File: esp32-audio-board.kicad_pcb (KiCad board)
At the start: 4 copper layers, 37.5 x 70 mm, 125 parts, among them IC1 LP2985A-33DBVR, J1 EN_PAD0, J10 PWR_LED+, J11 HP_LOUT1, J12 HP_ROUT1, J13 HP_LOUT2, J14 HP_ROUT2, J15 MIC_LIN1, J16 MIC_LIN1_GND, J17 MIC_RIN1, J18 MIC_RIN1_GND, J19 HP_GND1, J2 JST S2B, J20 HP_GND2, J21 VP_PAD0, J22 PWR_LED-, J23 CHG_LED+, J24 CHG_LED-, J3 USB_C_Receptacle_USB2.0_16P, J4 EN_PAD1, J5 VP_PAD1, J6 VN_PAD0, J7 VN_PAD1, J8 IO34_PAD0, J9 IO34_PAD1, Q1 SS8050, Q2 SS8050, Q4 AO3401A, U1 ESP32-WROOM-32E, U2 CP2102, U3 MCP73831-2-OT, U5 ES8388

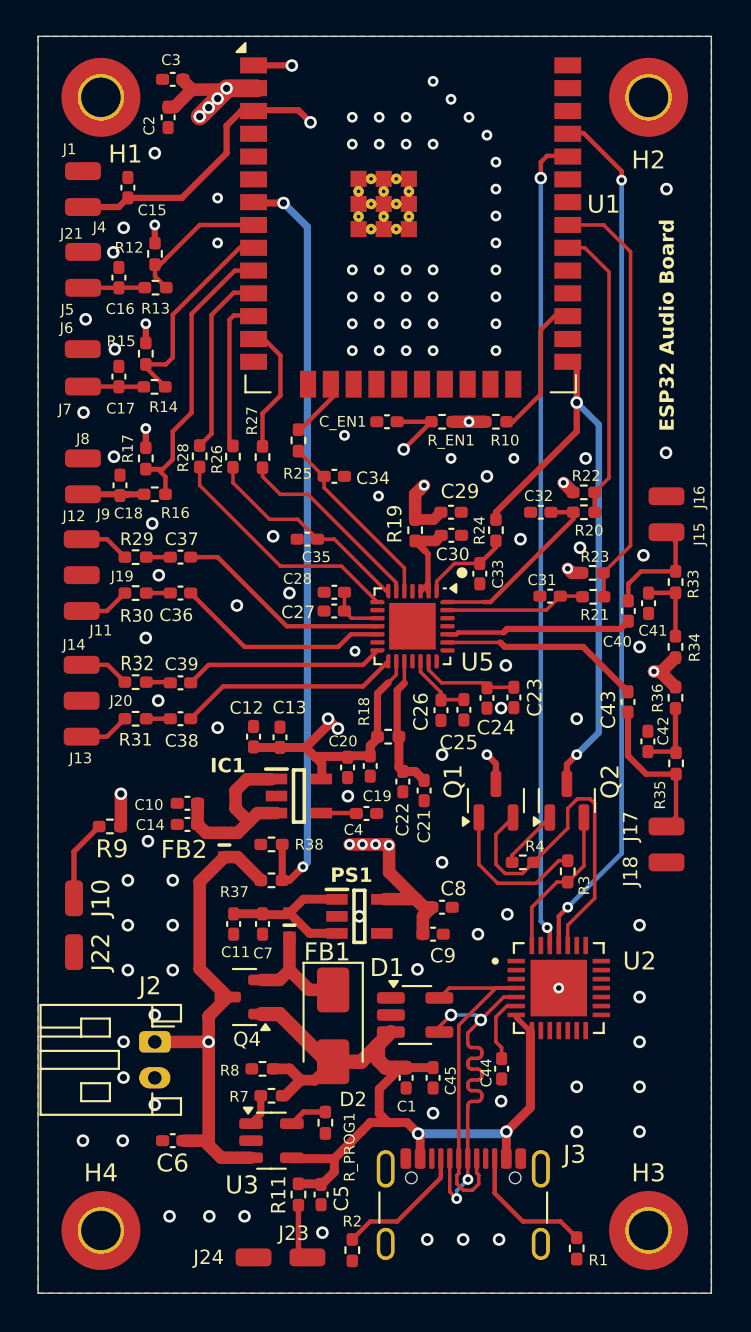
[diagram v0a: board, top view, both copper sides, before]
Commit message: esp32-audio-board: refactor PCB
Added many changes to the PCB, which hopefully
will protect the PCB from EMI even better and
will ensure that all signals have a short return
path to GND plane. Added pads for a boot button
to allow the board to be flashed even if the
auto-download circuit will not work.

Signed-off-by: RaresCon <rares.constantin2002@gmail.com>
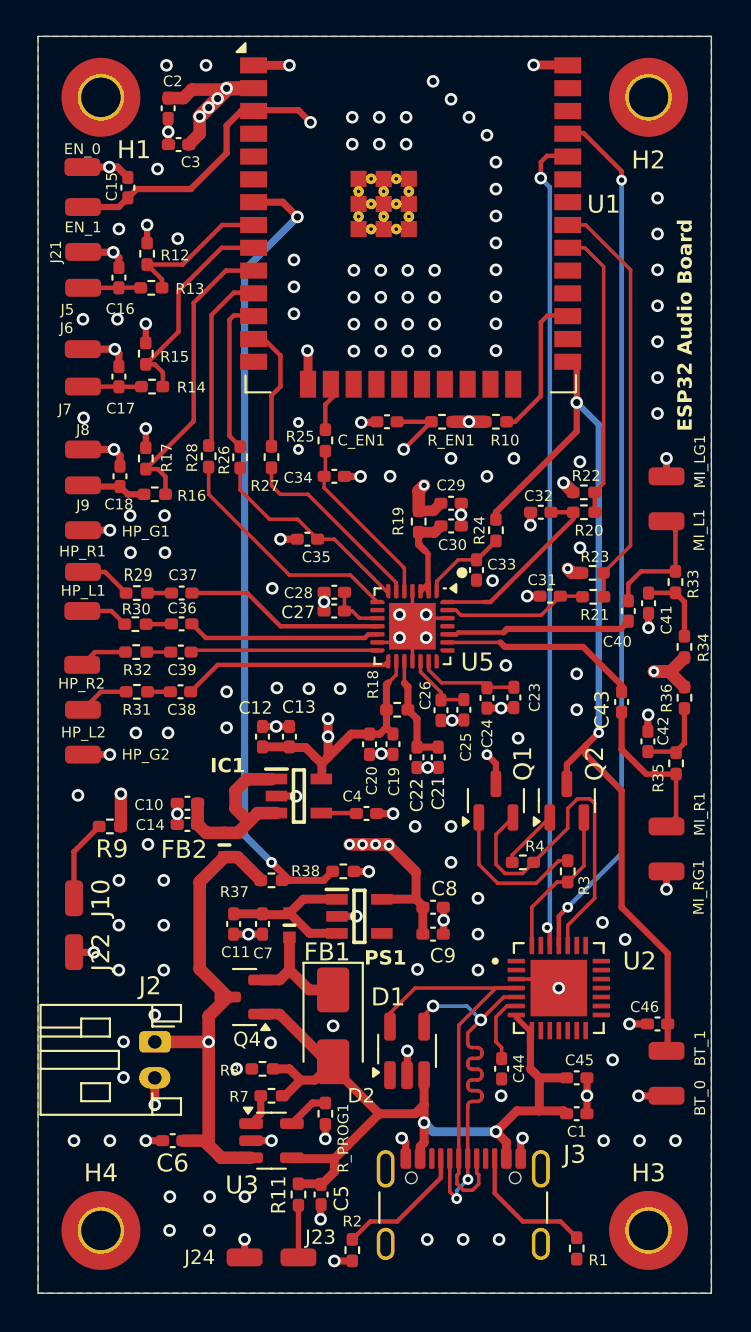
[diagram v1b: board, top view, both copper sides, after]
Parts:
- added BT_0: BOOT_PAD0, Connector_Wire:SolderWirePad_1x01_SMD_1x2mm, F.Cu at (67.5, 104.5)
- added BT_1: BOOT_PAD1, Connector_Wire:SolderWirePad_1x01_SMD_1x2mm, F.Cu at (67.5, 102.0)
- added C46: 0.1uF/10%, Capacitor_SMD:C_0402_1005Metric_Pad0.74x0.62mm_HandSolder, F.Cu at (67.0, 100.5)
- C_EN1: value 1uF/10% -> 0.1uF/10%
- J21: value VP_PAD0 -> IO32_PAD0
- J5: value VP_PAD1 -> IO32_PAD1
- J6: value VN_PAD0 -> IO33_PAD0
- J7: value VN_PAD1 -> IO33_PAD1
- J8: value IO34_PAD0 -> IO25_PAD0
- J9: value IO34_PAD1 -> IO25_PAD1
- moved C1 9.71 mm to (62.5, 105.5), turned to 0 degrees
- moved C45 8.00 mm to (62.5, 103.5), turned to 0 degrees
- moved R38 4.27 mm to (49.5, 92.0), turned to 0 degrees
- moved C3 3.65 mm to (40.3, 51.5)
- moved HP_G2 3.00 mm to (35.0, 85.5)
- moved HP_G1 2.50 mm to (35.0, 73.0)
- moved D1 2.05 mm to (53.0, 102.0), turned to 90 degrees
- moved C21 2.01 mm to (54.8, 85.6)
- moved C37 2.00 mm to (40.5, 76.5)
- moved R29 2.00 mm to (38.0, 76.5)
- moved HP_R1 1.82 mm to (35.0, 75.3)
- moved C20 1.78 mm to (51.0, 84.9)
- moved C19 1.76 mm to (52.3, 84.9)
- moved R30 1.73 mm to (37.9, 78.2)
- moved C36 1.72 mm to (40.5, 78.2)
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- renumbered J1 to EN_0, J4 to EN_1, J19 to HP_G1, J20 to HP_G2, J11 to HP_L1, J13 to HP_L2, J12 to HP_R1, J14 to HP_R2, J15 to MI_L1, J16 to MI_LG1, J17 to MI_R1, J18 to MI_RG1
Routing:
- net GND: track 2.84 -> 74.1 mm, vias 106 -> 167
- net ESP-IO0: track 33.3 -> 52.2 mm
- net /D+: track 20.4 -> 24.3 mm
- net ESP-EN: track 66.0 -> 68.4 mm
- net ESP_IO35: track 42.8 -> 45.0 mm
- net +3V3: track 120.2 -> 122.0 mm
- net +3V3 Audio: track 75.8 -> 77.2 mm
- net Net-(U5-AVDD): track 7.82 -> 6.40 mm
- net /D-: track 21.7 -> 23.1 mm
- net ES8388_LOUT1: track 11.9 -> 10.7 mm
- net ES8388_ROUT1: track 12.0 -> 11.1 mm
- net ES8388_ROUT2: track 11.1 -> 10.4 mm
- net BCK: track 3.48 -> 2.80 mm
- net ES8388_LOUT2: track 12.3 -> 11.7 mm
- net Net-(MI_L1-Pin_1): track 6.34 -> 6.94 mm
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
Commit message: esp32-audio-board: add bigger pads for pins
Added two new pads for audio pins and button pins
to allow larger cables to be soldered to the board.

Signed-off-by: RaresCon <rares.constantin2002@gmail.com>
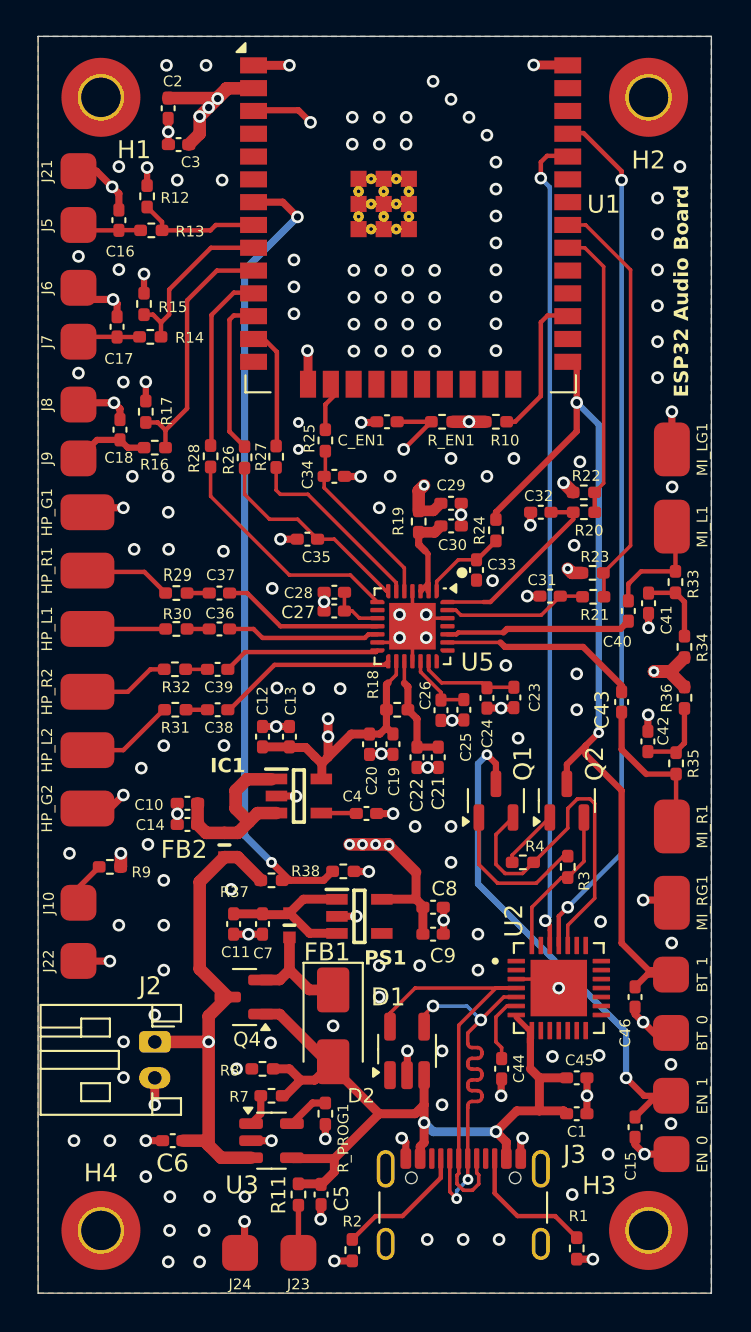
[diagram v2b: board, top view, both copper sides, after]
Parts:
- BT_0, BT_1, EN_0, EN_1, J10, J21, J22, J23, J24, J5, J6, J7, J8, J9: footprint Connector_Wire:SolderWirePad_1x01_SMD_1x2mm -> solderpads:SolderPad_SMD_2x2mm
- HP_G1, HP_G2, HP_L1, HP_L2, HP_R1, HP_R2, MI_L1, MI_LG1, MI_R1, MI_RG1: footprint Connector_Wire:SolderWirePad_1x01_SMD_1x2mm -> solderpads:SolderPad_SMD_2x3mm
- moved EN_0 64.0 mm to (67.8, 107.8), turned to -90 degrees
- moved C15 59.5 mm to (65.8, 106.2), turned to -90 degrees
- moved EN_1 59.4 mm to (67.8, 104.5), turned to -90 degrees
- moved J21 4.51 mm to (34.8, 53.0)
- moved BT_1 4.26 mm to (67.8, 97.8)
- moved J5 3.51 mm to (34.8, 56.0)
- moved BT_0 3.51 mm to (67.8, 101.0)
- moved J6 3.42 mm to (34.8, 59.5)
- moved C16 3.20 mm to (37.0, 55.7)
- moved R12 3.20 mm to (38.6, 54.4)
- moved R13 3.20 mm to (38.8, 56.3)
- moved HP_G2 3.01 mm to (35.2, 88.5), turned to 180 degrees
- moved C17 2.77 mm to (36.9, 61.7)
- moved R14 2.77 mm to (38.7, 62.2)
- moved R15 2.77 mm to (38.4, 60.4)
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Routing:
- net ESP-EN: track 68.4 -> 82.9 mm, vias 3 -> 4
- net GND: track 74.1 -> 82.5 mm, vias 167 -> 178
- net Net-(HP_L2-Pin_1): track 2.82 -> 5.23 mm
- net ESP_IO25: track 16.7 -> 14.4 mm
- net ESP_IO33: track 11.9 -> 9.62 mm
- net ES8388_LOUT1: track 10.7 -> 8.52 mm
- net Net-(J10-Pin_1): track 4.58 -> 2.48 mm
- net ES8388_ROUT1: track 11.1 -> 9.00 mm
- net Net-(HP_R1-Pin_1): track 2.89 -> 4.87 mm
- net Net-(HP_R2-Pin_1): track 2.71 -> 4.67 mm
- net Net-(HP_L1-Pin_1): track 2.66 -> 4.35 mm
- net ESP-IO0: track 52.2 -> 50.5 mm
- net ES8388_ROUT2: track 10.4 -> 8.77 mm
- net ES8388_LOUT2: track 11.7 -> 10.1 mm
- net ESP_IO32: track 8.49 -> 6.87 mm
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
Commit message: esp32-audio-board: add testpoints and tweaks
Added testpoints for SDA/SCL lines to allow for
rising edge refinements if needed for ES8388.
Checked all the decoupling capacitors and viases
for mistakes, fixed (hopefully) all of them.

Sent the board in production!

Signed-off-by: RaresCon <rares.constantin2002@gmail.com>
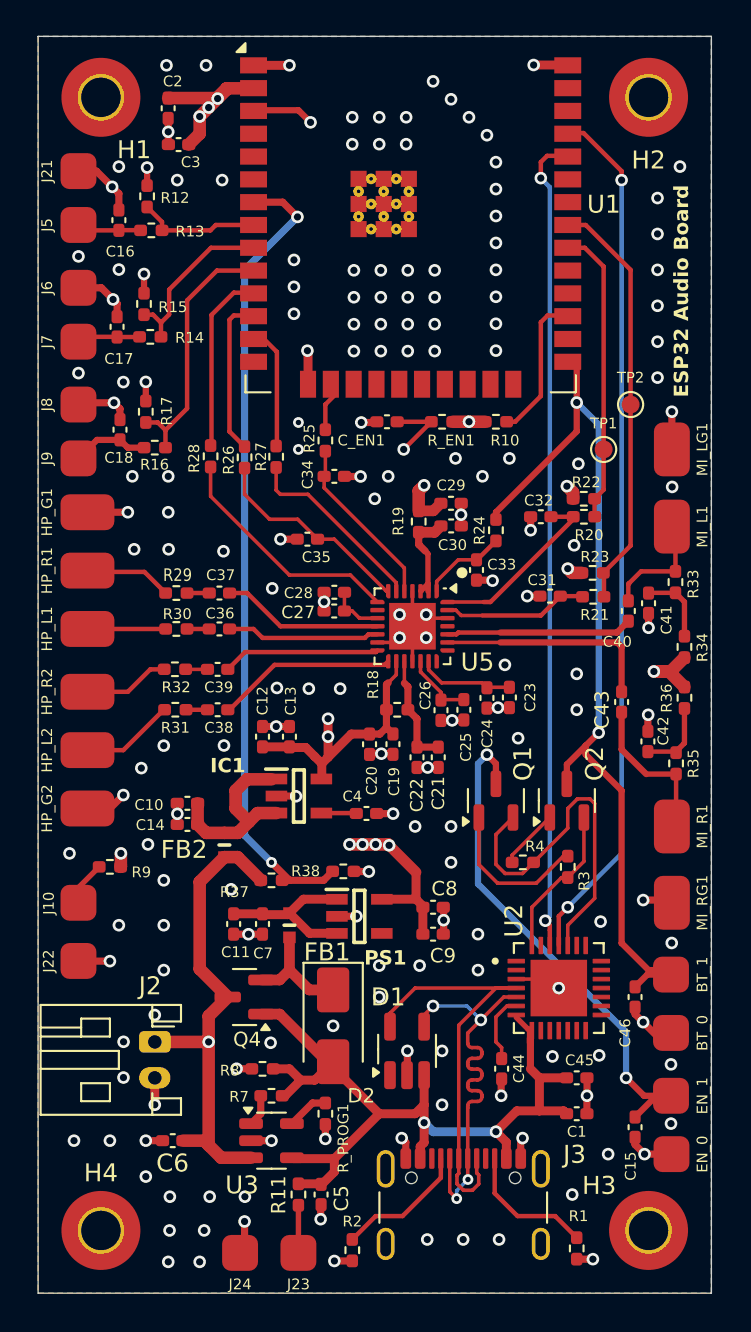
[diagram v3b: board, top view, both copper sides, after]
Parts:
- added TP1: T_SCL, TestPoint:TestPoint_Pad_D1.0mm, F.Cu at (64.0, 68.5)
- added TP2: T_SDA, TestPoint:TestPoint_Pad_D1.0mm, F.Cu at (65.5, 66.0)
- C_EN1: value 0.1uF/10% -> 1uF/10%
- moved R22 0.36 mm to (62.9, 71.2)
- moved C23 0.25 mm to (58.8, 82.3)
- moved C32 0.25 mm to (60.5, 72.2)
- moved R20 0.25 mm to (62.9, 72.2)
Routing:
- net GND: track 82.5 -> 84.4 mm
- net ES8388_RIN1: track 11.0 -> 12.3 mm

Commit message: esp32-audio-board: fix VI for audio pwr
The audio 3V3 was coming directly from the battery, which
may not be present and the VBUS should power the audio
circuits. The production board has this problem, but it
should not be affected if a battery is plugged in, as
the battery voltage will be present and the battery will
power the audio circuits correctly even when charging.

The charging led is now hooked correctly to the charger
IC on the STAT pin.

Signed-off-by: RaresCon <rares.constantin2002@gmail.com>
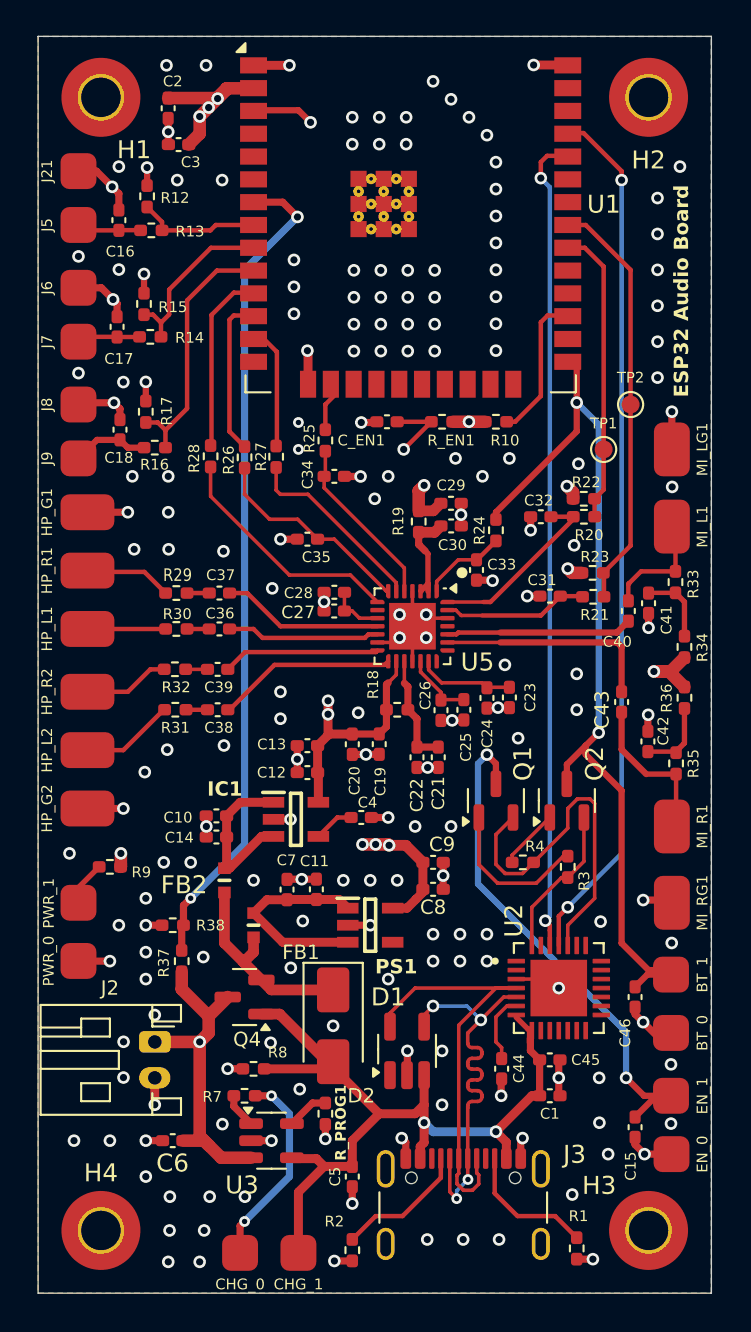
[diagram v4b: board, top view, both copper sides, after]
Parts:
- removed R11: 1K/1%, Resistor_SMD:R_0402_1005Metric_Pad0.72x0.64mm_HandSolder
- moved R38 9.96 mm to (40.0, 95.0), turned to 180 degrees
- moved R37 6.73 mm to (40.5, 97.0), turned to 90 degrees
- moved C11 5.00 mm to (48.0, 93.0), turned to 90 degrees
- moved C9 4.00 mm to (54.5, 91.5)
- moved C12 3.20 mm to (47.5, 86.5), turned to 180 degrees
- moved C7 2.35 mm to (46.4, 93.0), turned to 90 degrees
- moved C5 2.01 mm to (50.0, 109.0)
- moved FB1 2.00 mm to (44.5, 95.0)
- moved FB2 1.97 mm to (42.9, 92.5)
- moved C1 1.80 mm to (61.0, 104.5)
- moved C45 1.80 mm to (61.0, 102.5)
- moved C10 1.76 mm to (42.4, 88.9)
- moved C14 1.76 mm to (42.4, 90.1)
- moved R7 1.50 mm to (44.0, 104.5)
- moved IC1 1.31 mm to (46.9, 89.1)
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- renumbered J24 to CHG_0, J23 to CHG_1, J22 to PWR_0, J10 to PWR_1
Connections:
- CHG_0 pad 1: GND -> Net-(CHG_0-Pin_1)
- CHG_1 pad 1: Net-(J23-Pin_1) -> VBUS
- FB2 pad 1: VBAT -> VI
- R7 pad 2: VBUS -> Net-(CHG_0-Pin_1)
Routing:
- net Net-(CHG_0-Pin_1): track 0.00 -> 11.2 mm, vias 0 -> 2
- net VBAT: track 27.5 -> 18.9 mm
- net VI: track 6.51 -> 11.6 mm
- net Net-(PS1-EN): track 8.95 -> 11.7 mm
- net Net-(J23-Pin_1): track 2.65 -> 0.00 mm
- net +3V3: track 122.5 -> 119.9 mm, vias 12 -> 11
- net GND: track 84.4 -> 82.7 mm, vias 178 -> 187
- net VBUS: track 49.4 -> 47.9 mm
- net ESP_IO35: track 45.0 -> 46.3 mm
- net Net-(IC1-ON/~{OFF}): track 10.5 -> 9.35 mm
- net +3V3 Audio: track 77.2 -> 76.1 mm
